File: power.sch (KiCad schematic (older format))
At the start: 18 parts, among them J201 Power_Planes, Q201 Q_PMOS_GSD, U201 TLV75733PDRV

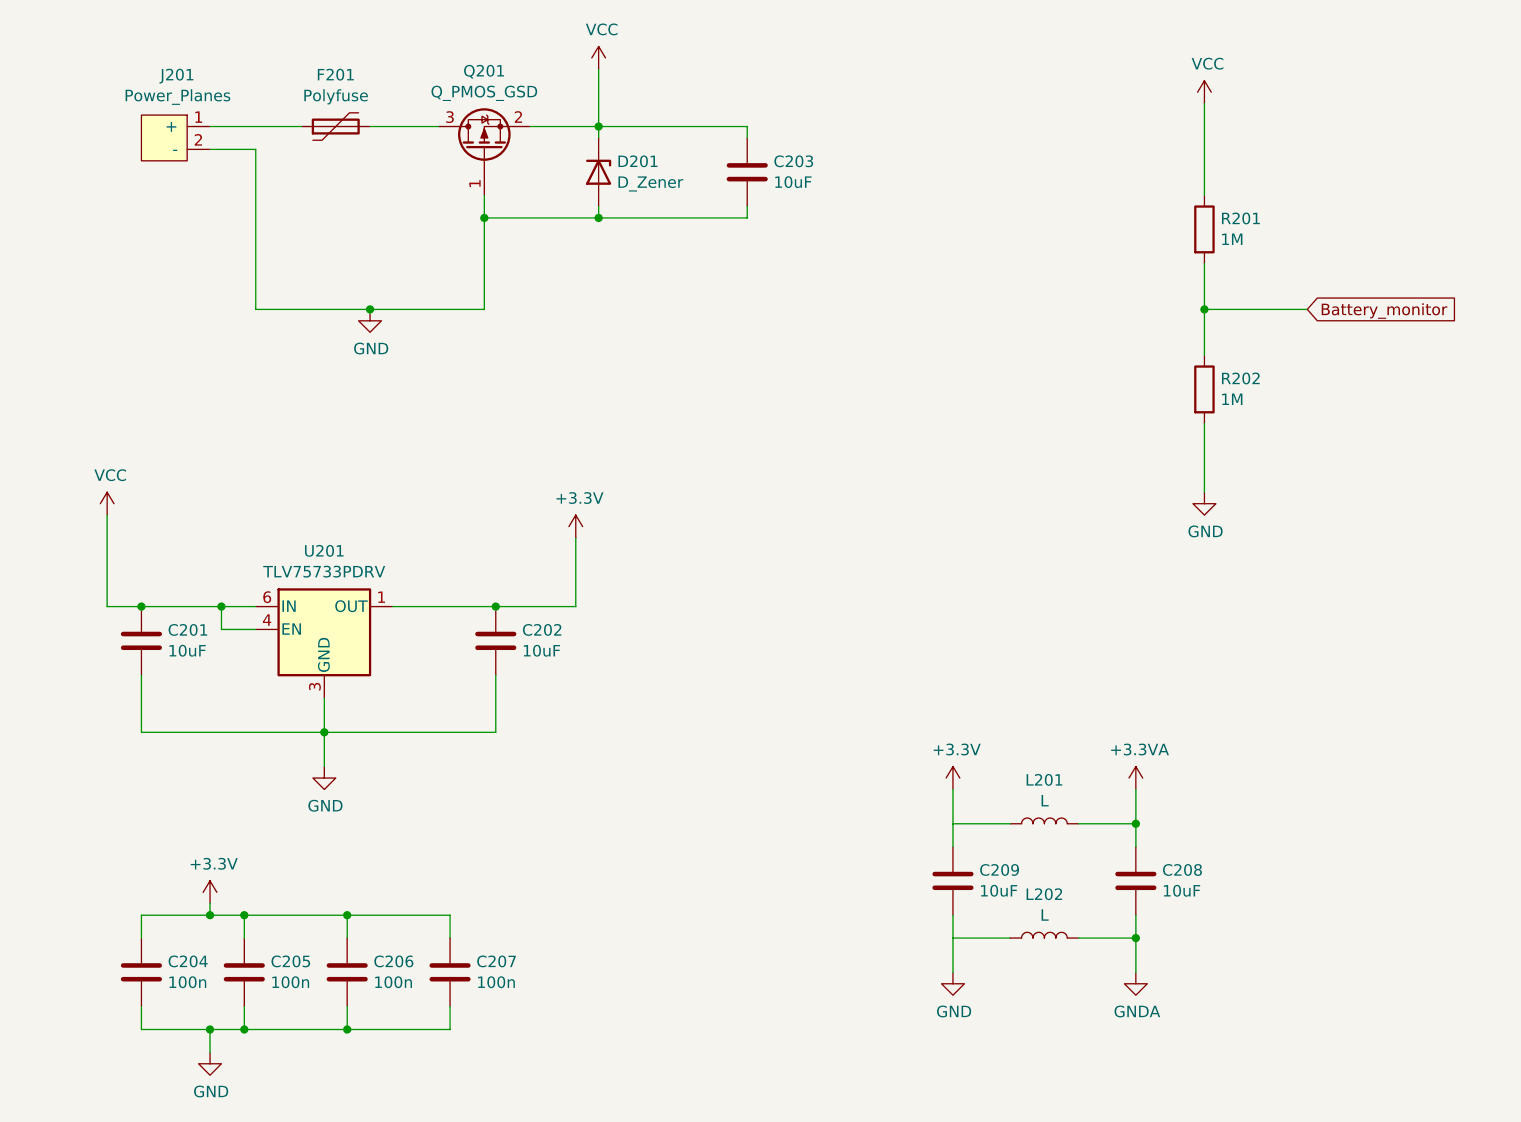
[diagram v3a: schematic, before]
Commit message: Added more filtering. Placed bypass caps near esp32 power intake.
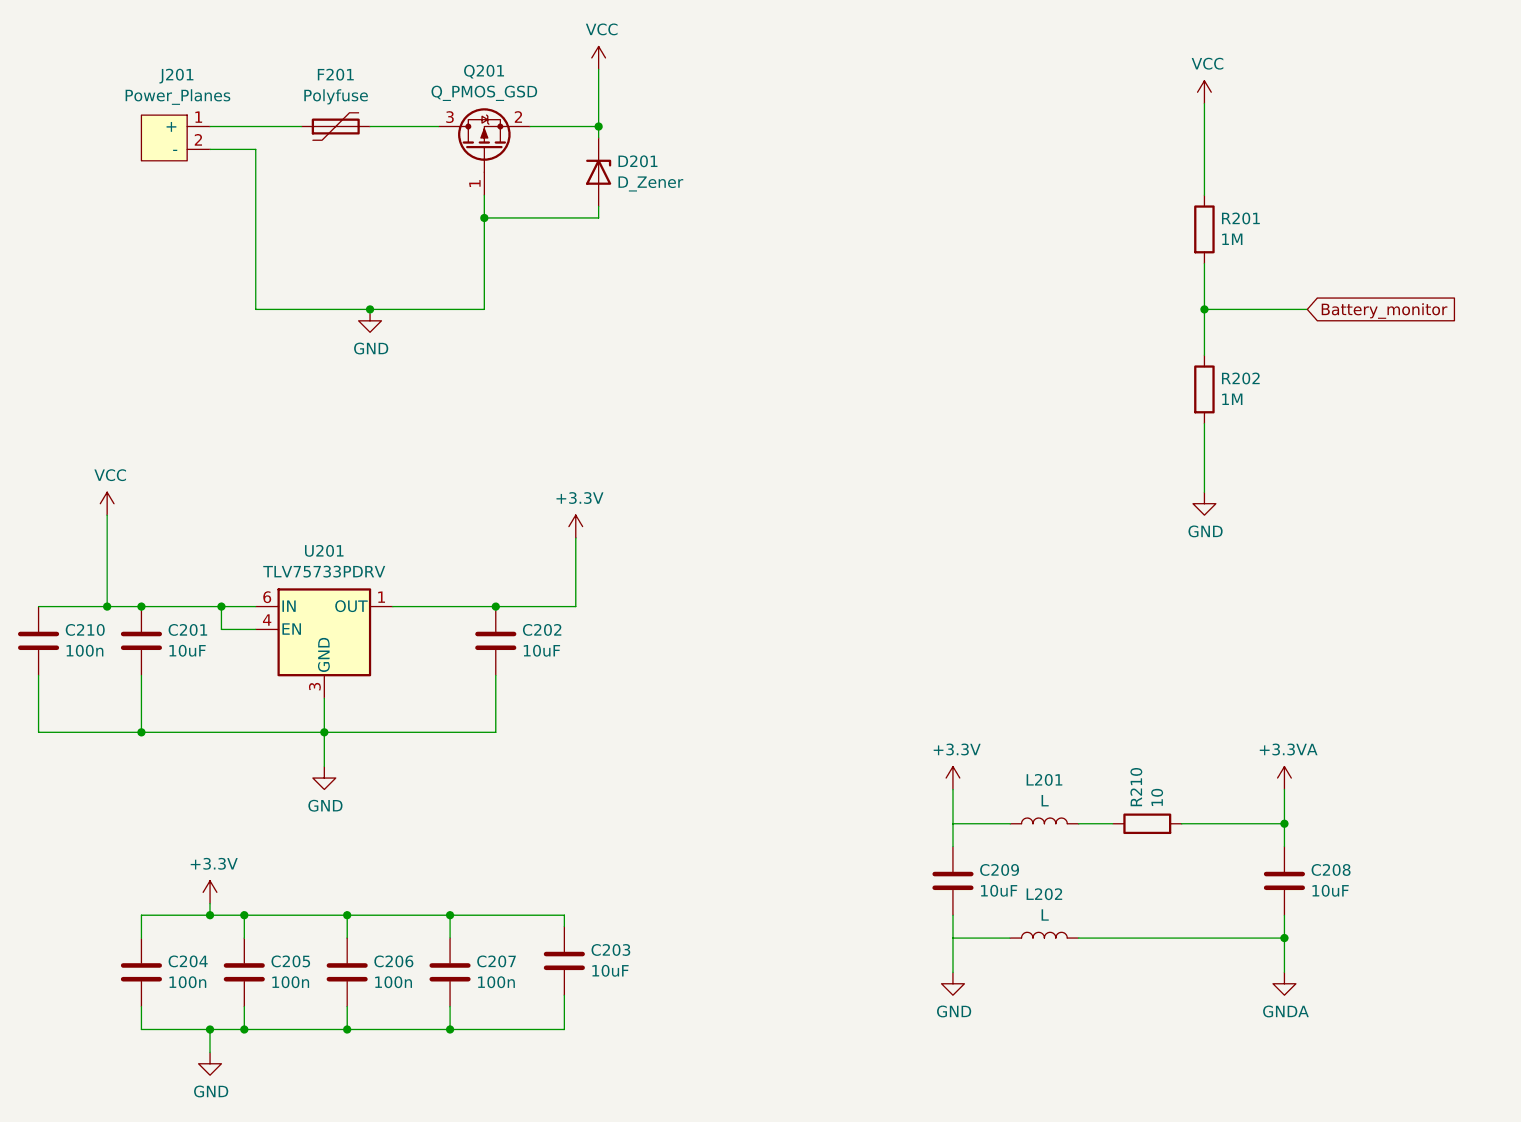
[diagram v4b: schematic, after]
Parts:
- added C210: 100n, Capacitor_SMD:C_0603_1608Metric_Pad1.08x0.95mm_HandSolder, symbol Device:C
- added R210: 10, Resistor_SMD:R_1206_3216Metric_Pad1.30x1.75mm_HandSolder, symbol Device:R
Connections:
- net +3.3VA: now also R210.2; no longer L201.2
- net +3V3: now also C203.1
- net GND: now also C210.2
- net VCC: now also C210.1; no longer C203.1
- new net: L201.2, R210.1
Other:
- moved on the sheet: C203, C208
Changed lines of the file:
@@
 Wire Wire Line
 	1750 3850 1750 3600
-Wire Wire Line
-	1600 3300 1750 3300
 Connection ~ 1750 3300
 Wire Wire Line
@@
 L Device:C C203
 U 1 1 615D867C
-P 4400 1400
-F 0 "C203" H 4515 1446 50  0000 L CNN
-F 1 "10uF" H 4515 1355 50  0000 L CNN
-F 2 "Capacitor_SMD:C_1206_3216Metric" H 4438 1250 50  0001 C CNN
-F 3 "~" H 4400 1400 50  0001 C CNN
-	1    4400 1400
+P 3600 4850
+F 0 "C203" H 3715 4896 50  0000 L CNN
+F 1 "10uF" H 3715 4805 50  0000 L CNN
+F 2 "Capacitor_SMD:C_1206_3216Metric" H 3638 4700 50  0001 C CNN
+F 3 "~" H 3600 4850 50  0001 C CNN
+	1    3600 4850
 	1    0    0    -1
 $EndComp
@@
 Connection ~ 2650 5150
 Wire Wire Line
-	3750 1600 4400 1600
-Wire Wire Line
-	4400 1600 4400 1550
-Connection ~ 3750 1600
-Wire Wire Line
-	4400 1250 4400 1200
-Wire Wire Line
-	4400 1200 3750 1200
-$Comp
-L power:+3.3VA #PWR?
-U 1 1 615ECA84
-P 6100 4100
-AR Path="/615ECA84" Ref="#PWR?"  Part="1"
-AR Path="/6099554C/615ECA84" Ref="#PWR?"  Part="1"
-AR Path="/609974E9/615ECA84" Ref="#PWR0205"  Part="1"
-F 0 "#PWR0205" H 6100 3950 50  0001 C CNN
-F 1 "+3.3VA" H 6115 4273 50  0000 C CNN
-F 2 "" H 6100 4100 50  0001 C CNN
-F 3 "" H 6100 4100 50  0001 C CNN
-	1    6100 4100
-	1    0    0    -1
-$EndComp
-$Comp
-L power:GNDA #PWR?
-U 1 1 615ECA8A
-P 6100 4900
-AR Path="/615ECA8A" Ref="#PWR?"  Part="1"
-AR Path="/6099554C/615ECA8A" Ref="#PWR?"  Part="1"
-AR Path="/609974E9/615ECA8A" Ref="#PWR0206"  Part="1"
-F 0 "#PWR0206" H 6100 4650 50  0001 C CNN
-F 1 "GNDA" H 6105 4727 50  0000 C CNN
-F 2 "" H 6100 4900 50  0001 C CNN
-F 3 "" H 6100 4900 50  0001 C CNN
-	1    6100 4900
-	1    0    0    -1
-$EndComp
+	3600 4700 3600 4650
 $Comp
 L power:+3.3V #PWR0203
@@
 	0    -1   -1   0
 $EndComp
+Wire Wire Line
+	5300 4100 5300 4250
+Wire Wire Line
+	5300 4250 5550 4250
+Wire Wire Line
+	5300 4750 5300 4900
+$Comp
+L Device:C C209
+U 1 1 6162616F
+P 5300 4500
+F 0 "C209" H 5415 4546 50  0000 L CNN
+F 1 "10uF" H 5415 4455 50  0000 L CNN
+F 2 "Capacitor_SMD:C_1206_3216Metric" H 5338 4350 50  0001 C CNN
+F 3 "~" H 5300 4500 50  0001 C CNN
+	1    5300 4500
+	1    0    0    -1
+$EndComp
+Wire Wire Line
+	5300 4350 5300 4250
+Wire Wire Line
+	5300 4650 5300 4750
+Wire Wire Line
+	5550 4750 5300 4750
 $Comp
 L Device:L L202
@@
 	0    -1   -1   0
 $EndComp
-Wire Wire Line
-	5300 4100 5300 4250
-Wire Wire Line
-	5300 4250 5550 4250
-Wire Wire Line
-	5550 4750 5300 4750
-Wire Wire Line
-	5300 4750 5300 4900
+$Comp
+L power:+3.3VA #PWR?
+U 1 1 615ECA84
+P 6750 4100
+AR Path="/615ECA84" Ref="#PWR?"  Part="1"
+AR Path="/6099554C/615ECA84" Ref="#PWR?"  Part="1"
+AR Path="/609974E9/615ECA84" Ref="#PWR0205"  Part="1"
+F 0 "#PWR0205" H 6750 3950 50  0001 C CNN
+F 1 "+3.3VA" H 6765 4273 50  0000 C CNN
+F 2 "" H 6750 4100 50  0001 C CNN
+F 3 "" H 6750 4100 50  0001 C CNN
+	1    6750 4100
+	1    0    0    -1
+$EndComp
+$Comp
+L power:GNDA #PWR?
+U 1 1 615ECA8A
+P 6750 4900
+AR Path="/615ECA8A" Ref="#PWR?"  Part="1"
+AR Path="/6099554C/615ECA8A" Ref="#PWR?"  Part="1"
+AR Path="/609974E9/615ECA8A" Ref="#PWR0206"  Part="1"
+F 0 "#PWR0206" H 6750 4650 50  0001 C CNN
+F 1 "GNDA" H 6755 4727 50  0000 C CNN
+F 2 "" H 6750 4900 50  0001 C CNN
+F 3 "" H 6750 4900 50  0001 C CNN
+	1    6750 4900
+	1    0    0    -1
+$EndComp
 $Comp
 L Device:C C208
 U 1 1 6160932C
-P 6100 4500
-F 0 "C208" H 6215 4546 50  0000 L CNN
-F 1 "10uF" H 6215 4455 50  0000 L CNN
-F 2 "Capacitor_SMD:C_1206_3216Metric" H 6138 4350 50  0001 C CNN
-F 3 "~" H 6100 4500 50  0001 C CNN
-	1    6100 4500
-	1    0    0    -1
-$EndComp
-Wire Wire Line
-	5850 4250 6100 4250
-Wire Wire Line
-	6100 4250 6100 4100
-Wire Wire Line
-	6100 4350 6100 4250
-Connection ~ 6100 4250
-Wire Wire Line
-	6100 4650 6100 4750
-Wire Wire Line
-	5850 4750 6100 4750
-Connection ~ 6100 4750
-Wire Wire Line
-	6100 4750 6100 4900
-$Comp
-L Device:C C209
-U 1 1 6162616F
-P 5300 4500
-F 0 "C209" H 5415 4546 50  0000 L CNN
-F 1 "10uF" H 5415 4455 50  0000 L CNN
-F 2 "Capacitor_SMD:C_1206_3216Metric" H 5338 4350 50  0001 C CNN
-F 3 "~" H 5300 4500 50  0001 C CNN
-	1    5300 4500
-	1    0    0    -1
-$EndComp
-Wire Wire Line
-	5300 4350 5300 4250
-Wire Wire Line
-	5300 4650 5300 4750
+P 6750 4500
+F 0 "C208" H 6865 4546 50  0000 L CNN
+F 1 "10uF" H 6865 4455 50  0000 L CNN
+F 2 "Capacitor_SMD:C_1206_3216Metric" H 6788 4350 50  0001 C CNN
+F 3 "~" H 6750 4500 50  0001 C CNN
+	1    6750 4500
+	1    0    0    -1
+$EndComp
+Wire Wire Line
+	6750 4250 6750 4100
+Wire Wire Line
+	6750 4350 6750 4250
+Connection ~ 6750 4250
+Wire Wire Line
+	6750 4650 6750 4750
+Connection ~ 6750 4750
+Wire Wire Line
+	6750 4750 6750 4900
+Wire Wire Line
+	5850 4750 6750 4750
+$Comp
+L Device:R R210
+U 1 1 615F098E
+P 6150 4250
+F 0 "R210" H 6220 4296 50  0000 L CNN
+F 1 "10" H 6220 4205 50  0000 L CNN
+F 2 "Resistor_SMD:R_1206_3216Metric_Pad1.30x1.75mm_HandSolder" V 6080 4250 50  0001 C CNN
+F 3 "~" H 6150 4250 50  0001 C CNN
+	1    6150 4250
+	0    -1   -1   0
+$EndComp
+Wire Wire Line
+	6300 4250 6750 4250
+Wire Wire Line
+	5850 4250 6000 4250
+Connection ~ 3100 4650
+Wire Wire Line
+	3600 4650 3100 4650
+Wire Wire Line
+	3100 5150 3600 5150
+Connection ~ 3100 5150
+Wire Wire Line
+	3600 5000 3600 5150
+$Comp
+L Device:C C210
+U 1 1 6160E0E7
+P 1300 3450
+F 0 "C210" H 1415 3496 50  0000 L CNN
+F 1 "100n" H 1415 3405 50  0000 L CNN
+F 2 "Capacitor_SMD:C_0603_1608Metric_Pad1.08x0.95mm_HandSolder" H 1338 3300 50  0001 C CNN
+F 3 "~" H 1300 3450 50  0001 C CNN
+	1    1300 3450
+	1    0    0    -1
+$EndComp
+Wire Wire Line
+	1300 3300 1600 3300
+Connection ~ 1600 3300
+Wire Wire Line
+	1600 3300 1750 3300
+Wire Wire Line
+	1300 3600 1300 3850
+Wire Wire Line
+	1300 3850 1750 3850
+Connection ~ 1750 3850
 $EndSCHEMATC
